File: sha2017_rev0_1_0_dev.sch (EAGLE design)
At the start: 184 parts, among them IC1 AP7215, IC2 CPT112, IC3 CP210X_USB_UART, IC4 ESP32WROOM32, IC5 MCP73833, IC6 FXL6408, Q1 MMBT2222A, Q2 MMBT2222A, Q3 SI1304 BDL, Q4 MOSFET-PCHANNEL, Q5 MMBT2222A, Q6 MOSFET-PCHANNEL, Q7 MMBT2222A, Q8 MMBT2222A, T1 SI2301DS, X1_ JST-PH3, X701 2908-05WB-MG

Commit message: renumbered PCB and placed designators
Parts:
- removed D14: NSVR0320MW2T1G, SparkFun-DiscreteSemi:BAT20JFILM
- removed U$29, U$30: VIA, badge:VIA
- added $$U$7, $$U$9: VIA, badge:VIA
- added D8: NSVR0320MW2T1G, SparkFun-DiscreteSemi:BAT20JFILM
- C1, C5: PARTNO GRM188R71H104KA93D -> (none)
- C10: value 1u -> 100n; PARTNO GRM188R61E105KA12D -> (none)
- C12, C14, C17, C7: value 1u -> 4u7/16V; device rcl:C-EUC0603 -> rcl:C-EUC0805; PARTNO GRM188R61E105KA12D -> GRM21BR61C475KA88K
- C13: value 1u -> 100n; OC_FARNELL (none) -> unknown; PARTNO GRM188R61E105KA12D -> (none)
- C15: value 100n -> 4u7/16V; device rcl:C-EUC0603 -> rcl:C-EUC0805; PARTNO GRM188R71H104KA93D -> GRM21BR61C475KA88K
- C16, C22: value 4u7/16V -> 1u; device rcl:C-EUC0805 -> rcl:C-EUC0603; PARTNO GRM21BR61C475KA88K -> GRM188R61E105KA12D
- C19, C9: value 1u -> 100n; PARTNO GRM188R61E105KA12D -> GRM188R71H104KA93D
- C2, C4: value 4u7/16V -> 100n; device rcl:C-EUC0805 -> rcl:C-EUC0603; PARTNO GRM21BR61C475KA88K -> (none)
- C20: value (none) -> 10uF; device rcl:C-EUC0603 -> rcl:C-EUC0805K; OC_FARNELL unknown -> (none)
- C21: value (none) -> 100nF; device rcl:C-EUC0603 -> rcl:C-EUC0402K; OC_FARNELL unknown -> (none)
- C25: value 10uF -> (none); device rcl:C-EUC0805K -> rcl:C-EUC0603; OC_FARNELL (none) -> unknown
- C26: value 100n -> (none); OC_FARNELL (none) -> unknown
- C27: value 100n -> 4u7/16V; device rcl:C-EUC0603 -> rcl:C-EUC0805; PARTNO (none) -> GRM21BR61C475KA88K
- C28, C29: value 100n -> 1u; PARTNO (none) -> GRM188R61E105KA12D
- C3: device rcl:C-EUC0805 -> 00ralf:C0603-DASHES; PARTNO GRM21BR61C475KA88K -> (none)
- C30: value 100n -> 10uF; device rcl:C-EUC0603 -> rcl:C-EUC0805K
- C31: value 4u7/16V -> 1u; device 00ralf:C0603-DASHES -> rcl:C-EUC0603; PARTNO (none) -> GRM188R61E105KA12D
- C32: value 10uF -> 1u; device rcl:C-EUC0805K -> rcl:C-EUC0603; PARTNO (none) -> GRM188R61E105KA12D
- C33: value 100nF -> 1u; device rcl:C-EUC0402K -> rcl:C-EUC0603; PARTNO (none) -> GRM188R61E105KA12D
- C34: value 100n -> 1u; OC_FARNELL unknown -> (none); PARTNO (none) -> GRM188R61E105KA12D
- C36: value 100n -> 4u7/16V; device rcl:C-EUC0603 -> 00ralf:C0603-DASHES; OC_FARNELL unknown -> (none)
- C37: value 4u7/16V -> (none); device 00ralf:C0603-DASHES -> rcl:C-EUC0603; OC_FARNELL (none) -> unknown
- C38: value (none) -> 100n; OC_FARNELL unknown -> (none); PARTNO (none) -> GRM188R71H104KA93D
- C8: value 4u7/16V -> 100n; device rcl:C-EUC0805 -> rcl:C-EUC0603; OC_FARNELL (none) -> unknown; PARTNO GRM21BR61C475KA88K -> (none)
- D2: PARTNO BAT20JFILM -> (none)
- D3: value NSVR0320MW2T1G -> Yellow; device SparkFun-DiscreteSemi:BAT20JFILM -> SparkFun-LED:LED0603; PARTNO BAT20JFILM -> (none)
- D4: value Yellow -> RED
- D6: value RED -> NSVR0320MW2T1G; device SparkFun-LED:LED0603 -> SparkFun-DiscreteSemi:BAT20JFILM; PARTNO (none) -> BAT20JFILM
- IC1: value AP7215 -> CP210X_USB_UART; device badge:AP7215 -> SparkFun-DigitalIC:CP210X_USB_UART; PARTNO AP7215-33YG-13 -> CP2102-GMR
- IC2: value CPT112 -> AP7215; device badge:CPT112 -> badge:AP7215; PARTNO (none) -> AP7215-33YG-13
- IC3: value CP210X_USB_UART -> ESP32WROOM32; device SparkFun-DigitalIC:CP210X_USB_UART -> ESP3x:ESP32WROOM32; PARTNO CP2102-GMR -> (none)
- IC4: value ESP32WROOM32 -> MCP73833; device ESP3x:ESP32WROOM32 -> SparkFun:MCP73833
- IC5: value MCP73833 -> FXL6408; device SparkFun:MCP73833 -> badge:FXL6408
- IC6: value FXL6408 -> CPT112; device badge:FXL6408 -> badge:CPT112
- Q1: value MMBT2222A -> MOSFET-PCHANNEL; device SparkFun-DiscreteSemi:TRANSISTOR_NPNMMBT2222A -> SparkFun-DiscreteSemi:MOSFET-PCHANNEL; PARTNO BC817-25,215 -> (none)
- Q2: PARTNO BC817-25,215 -> (none)
- Q3: value SI1304 BDL -> MMBT2222A; device SparkFun-DiscreteSemi:MOSFET-NCHANNEL2N7002PW -> SparkFun-DiscreteSemi:TRANSISTOR_NPNMMBT2222A; PARTNO SI1308EDL-T1-GE3 -> (none)
- Q4: value MOSFET-PCHANNEL -> MMBT2222A; device SparkFun-DiscreteSemi:MOSFET-PCHANNEL -> SparkFun-DiscreteSemi:TRANSISTOR_NPNMMBT2222A; PARTNO (none) -> BC817-25,215
- Q5: PARTNO (none) -> BC817-25,215
- Q6: value MOSFET-PCHANNEL -> SI1304 BDL; device SparkFun-DiscreteSemi:MOSFET-PCHANNEL -> SparkFun-DiscreteSemi:MOSFET-NCHANNEL2N7002PW; PARTNO (none) -> SI1308EDL-T1-GE3
- Q8: value MMBT2222A -> MOSFET-PCHANNEL; device SparkFun-DiscreteSemi:TRANSISTOR_NPNMMBT2222A -> SparkFun-DiscreteSemi:MOSFET-PCHANNEL
- R1: value 1k -> 10R; device rcl:R-EU_R0603 -> 00ralf:R0603-DASHES; PARTNO ERJ-3GEYJ102V -> (none)
- R10: value 100k -> 10k; PARTNO CRCW0603100KFKEA -> ERJ-3GEYJ103V
- R11: value 10k -> 1k; device 00ralf:R0603-DASHES -> rcl:R-EU_R0603; PARTNO (none) -> ERJ-3GEYJ102V
- R12: value 10R -> 10k; device 00ralf:R0603-DASHES -> rcl:R-EU_R0603; PARTNO (none) -> ERJ-3GEYJ103V
- R13: device 00ralf:R0603-DASHES -> rcl:R-EU_R0603; PARTNO (none) -> ERJ-3GEYJ103V
- R14: value 2.2k -> 10k; PARTNO (none) -> ERJ-3GEYJ103V
- R15: value 1k -> 5R; device rcl:R-EU_R0603 -> 00ralf:R0603-DASHES; PARTNO (none) -> ERJ-3GEYJ5R1V
- R16: value 10k -> 100k
- R18: device 00ralf:R0603-DASHES -> rcl:R-EU_R0603; OC_FARNELL (none) -> unknown; PARTNO (none) -> ERJ-3GEYJ103V
- R19: value 10k -> 470R; device 00ralf:R0603-DASHES -> rcl:R-EU_R0603; OC_FARNELL (none) -> unknown; PARTNO (none) -> ERJ-3GEYJ103V
- R20: value 100k -> 470R; OC_FARNELL (none) -> unknown; PARTNO (none) -> ERJ-3GEYJ103V
- R21: value 220k -> 10k; device rcl:R-EU_R0603 -> 00ralf:R0603-DASHES
- R22: value 100k -> 10k; device rcl:R-EU_R0603 -> 00ralf:R0603-DASHES
- R23: value 150k -> 2.2k
- R25: value 10k -> 100k; device 00ralf:R0603-DASHES -> rcl:R-EU_R0603; PARTNO (none) -> CRCW0603100KFKEA
- R26: value 10k -> 150k; OC_FARNELL unknown -> (none); PARTNO ERJ-3GEYJ103V -> (none)
- R27: value 470R -> 10k
- R28: value 470R -> 1k; OC_FARNELL unknown -> (none); PARTNO ERJ-3GEYJ103V -> (none)
- R3: PARTNO ERJ-3GEYJ103V -> (none)
- R4: value 1k -> 100k; PARTNO ERJ-3GEYJ102V -> (none)
- R5: value 10k -> 220k; PARTNO ERJ-3GEYJ103V -> (none)
- R6: device rcl:R-EU_R0603 -> 00ralf:R0603-DASHES; PARTNO ERJ-3GEYJ103V -> (none)
- R7: value 5R -> 10k; PARTNO ERJ-3GEYJ5R1V -> (none)
- R8: device rcl:R-EU_R0603 -> 00ralf:R0603-DASHES; OC_FARNELL unknown -> (none); PARTNO ERJ-3GEYJ103V -> (none)
- R9: value 10k -> 1k; PARTNO ERJ-3GEYJ103V -> ERJ-3GEYJ102V
- renumbered D10 to D101, D11 to D102, D12 to D103, D13 to D104, D9 to D100, J3 to J2, TB1 to TB104, TB2 to TB103, TB3 to TB101, TB4 to TB100, TB5 to TB102, TP10 to TP107, TP11 to TP106, TP12 to TP104, TP13 to TP105, TP14 to TP131, TP15 to TP130, TP16 to TP129, TP17 to TP127, TP18 to TP126, TP19 to TP125, TP20 to TP113, TP22 to TP114, TP23 to TP119, TP24 to TP120, TP25 to TP116, TP26 to TP115, TP27 to TP109, TP28 to TP118, TP29 to TP128, TP3 to TP100, TP30 to TP111, TP31 to TP132, TP32 to TP121, TP33 to TP133, TP34 to TP134, TP35 to TP137, TP36 to TP138, TP37 to TP108, TP38 to TP103, TP39 to TP124, TP4 to TP101, TP40 to TP135, TP41 to TP139, TP42 to TP102, TP43 to TP136, TP5 to TP123, TP6 to TP122, TP7 to TP117, TP8 to TP112, TP9 to TP110, U$31 to $$U$8, X1_ to X1, X701 to X2
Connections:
- net +3V3: now also C14.1, C17.1, C27.1, C34.1, C37.1, IC2.OUT, IC3.VCC, IC5.ADDR, IC5.VCC, IC5.VDDIO, IC6.VDD, Q8.D, R13.2, R18.1, R19.1, R20.1, R22.2, R25.1, R28.2; no longer C16.1, C22.1, C35.1, C4.1, C5.1, IC1.OUT, IC2.VDD, IC4.VCC, IC6.ADDR, IC6.VCC, IC6.VDDIO, Q6.D, R10.1, R24.2, R25.2, R26.1, R28.1, R8.1, R9.2
- net +5V: now also C20.2, C21.2, C7.1, C9.1, D2.A, IC1.REGIN, IC1.VBUS, IC4.VDD@1, IC4.VDD@2, R3.2, R5.2; no longer C11.1, C2.1, C32.2, C33.2, D14.A, IC3.REGIN, IC3.VBUS, IC5.VDD@1, IC5.VDD@2, R16.2, R21.2
- net 3V3_SWITCHED: now also C35.1, C36.1, Q8.S; no longer C15.1, C37.1, Q6.S
- net CHRG_STAT: now also IC4.STAT1, IC5.GPIO0; no longer IC5.STAT1, IC6.GPIO0
- net ESP32_!RESET: now also IC3.EN, Q4.C, R18.2, S1.2; no longer IC4.EN, Q1.C, R8.2, S2.2
- net ESP32_FLASH: now also IC3.IO0, Q5.C, R13.1, S2.2; no longer IC4.IO0, Q2.C, R9.1, S1.2
- net ESP32_RX: now also D3.C, IC1.TXD, IC3.RXD0; no longer D4.C, IC3.TXD, IC4.RXD0
- net ESP32_TX: now also D4.C, IC1.RXD, IC3.TXD0; no longer D6.C, IC3.RXD, IC4.TXD0
- net EXTIO-0: now also IC3.IO33; no longer IC4.IO33
- net EXTIO-1: now also IC3.IO16; no longer IC4.IO16
- net EXTIO-2: now also IC3.IO17; no longer IC4.IO17
- net EXTIO-3: now also IC5.GPIO7; no longer IC6.GPIO7
- net EXTIO-4: now also IC5.GPIO6; no longer IC6.GPIO6
- net EXTIO-5: now also IC5.GPIO5; no longer IC6.GPIO5
- net GDR: now also Q6.G; no longer Q3.G
- net GND: now also $$U$7.P$1, $$U$9.P$1, C1.1, C12.2, C13.2, C14.2, C16.1, C17.2, C2.1, C27.2, C31.1, C4.1, C5.1, C7.2, C9.2, D6.C, IC1.GND@EXP, IC1.GND@M, IC3.GND@0, IC3.GND@1, IC3.GND@3, IC4.VSS, IC5.GND, Q2.E, Q3.E, R15.2, R26.1, R3.1, R4.1; no longer C1.2, C12.1, C13.1, C16.2, C17.1, C2.2, C22.2, C27.1, C31.2, C4.2, C5.2, C7.1, C9.1, D3.C, IC3.GND@EXP, IC3.GND@M, IC4.GND, IC4.GND@0, IC4.GND@1, IC4.GND@3, IC5.VSS, Q5.E, Q8.E, R14.1, R20.1, R22.1, R7.2, U$29.P$1, U$30.P$1
- net I2C_INT: now also IC3.IO25, IC5.INT; no longer IC4.IO25, IC6.INT
- net I2C_SCL: now also IC3.IO27, IC5.SCL, IC6.EB_SCL, R20.2; no longer IC2.EB_SCL, IC4.IO27, IC6.SCL, R27.2
- net I2C_SDA: now also IC3.IO26, IC5.SDA, IC6.EB_SDA, R19.2; no longer IC2.EB_SDA, IC4.IO26, IC6.SDA, R28.2
- net LCD_!RESET: now also IC3.IO23; no longer IC4.IO23
- net LCD_BUSY: now also IC3.IO22; no longer IC4.IO22
- net LCD_CS: now also IC3.IO19; no longer IC4.IO19
- net LCD_D/!S: now also IC3.IO21; no longer IC4.IO21
- net LCD_MOSI: now also IC3.IO5; no longer IC4.IO5
- net LCD_SCK: now also IC3.IO18; no longer IC4.IO18
- net N$1: now also IC6.CS11/BUZZ; no longer IC2.CS11/BUZZ
- net N$10: now also IC1.RTS, Q4.E, R12.1; no longer IC3.RTS, Q1.E, R5.1
- net N$11: now also IC1.DTR, Q5.E, R14.1; no longer IC3.DTR, Q2.E, R6.1
- net N$12: now also IC3.SD1; no longer IC4.SD1
- net N$13: now also Q5.B, R12.2; no longer Q2.B, R5.2
- net N$14: now also Q4.B, R14.2; no longer Q1.B, R6.2
- net N$15: now also Q7.B, R21.2; no longer Q8.B, R11.2
- net N$16: now also Q3.C; no longer Q7.C
- net N$17: now also Q7.C, Q8.G, R22.1; no longer Q6.G, Q8.C, R25.1
- net N$18: now also R1.1; no longer R12.1
- net N$22: now also C22.1, D6.A, D7.C; no longer C14.1, D2.C, D3.A
- net N$23: now also C22.2, D8.A, Q6.D; no longer C14.2, D7.A, Q3.D
- net N$25: now also IC6.CS02; no longer IC2.CS02
- net N$26: now also R9.1; no longer R2.1
- net N$27: now also D3.A, R2.1; no longer D4.A, R1.1
- net N$28: now also D4.A, R11.1; no longer D6.A, R4.1
- net N$3: now also IC3.SD2; no longer IC4.SD2
- net N$4: now also IC3.SD3; no longer IC4.SD3
- net N$42: now also C25.2, IC3.SENSOR_VP; no longer C20.2, IC4.SENSOR_VP
- net N$43: now also C26.2, IC3.SENSOR_VN; no longer C21.2, IC4.SENSOR_VN
- net N$45: now also Q3.B, R8.1; no longer Q7.B, R13.1
- net N$46: now also IC4.PROG, R23.2; no longer IC5.PROG, R14.2
- net N$47: now also IC4.THERM, R24.2; no longer IC5.THERM, R15.2
- net N$48: now also R24.1, R26.2; no longer R15.1, R23.2
- net N$49: now also C30.2, IC4.VBAT@1, IC4.VBAT@2; no longer C25.2, IC5.VBAT@1, IC5.VBAT@2
- net N$52: now also Q2.B, R7.2; no longer Q5.B, R18.2
- net N$53: now also Q1.G, Q2.C, R6.1; no longer Q4.G, Q5.C, R19.1
- net N$55: now also IC6.CS03; no longer IC2.CS03
- net N$56: now also IC6.CS04; no longer IC2.CS04
- net N$57: now also IC6.CS05; no longer IC2.CS05
- net N$58: now also IC6.CS09; no longer IC2.CS09
- net N$59: now also IC5.!RESET, R27.2; no longer IC6.!RESET, R26.2
- net N$6: now also IC3.CND; no longer IC4.CND
- net N$61: now also IC6.CONF_CLK/RST, R28.1, TP2.1; no longer IC2.CONF_CLK/RST, R24.1, TP1.1
- net N$62: now also IC6.CONF_DAT, TP1.1; no longer IC2.CONF_DAT, TP2.1
- net N$64: now also IC6.CS08; no longer IC2.CS08
- net N$65: now also IC6.CS07; no longer IC2.CS07
- net N$7: now also IC3.CLK; no longer IC4.CLK
- net N$8: now also IC1.!RST, R10.2; no longer IC3.!RST, R3.2
- net N$9: now also IC3.SD0; no longer IC4.SD0
- net PREVGH: now also C28.2, D8.C; no longer C13.2, D7.C
- net PREVGL: now also C32.2, D7.A; no longer C9.2, D2.A
- net PROXIMITY: now also IC6.CS00; no longer IC2.CS00
- net RESE: now also Q6.S, R15.1; no longer Q3.S, R7.1
- net SD_CD: now also IC5.GPIO4, R25.2; no longer IC6.GPIO4, R10.2
- net SD_CLK: now also IC3.IO14; no longer IC4.IO14
- net SD_CMD: now also IC3.IO15; no longer IC4.IO15
- net SD_DATA0: now also IC3.IO2; no longer IC4.IO2
- net SD_DATA1: now also IC3.IO4; no longer IC4.IO4
- net SD_DATA2: now also IC3.IO12; no longer IC4.IO12
- net SD_DATA3: now also IC3.IO13; no longer IC4.IO13
- net TOUCH_INT: now also IC5.GPIO3, IC6.EB_INT; no longer IC2.EB_INT, IC6.GPIO3
- net USB_DN_CON: now also IC1.D-; no longer IC3.D-
- net USB_DP_CON: now also IC1.D+; no longer IC3.D+
- net VBAT_SENSE: now also C13.1, IC3.IO35, R16.2; no longer C34.1, IC4.IO35, R20.2
- net VCC: now also C11.1, C12.1, C15.1, D2.C, IC2.IN, Q1.D, R1.2, R6.2; no longer C1.1, C3.1, C8.1, D14.C, IC1.IN, Q4.D, R12.2, R19.2
- net VCOM: now also C33.2; no longer C7.2
- net VDD: now also IC1.VDD, R10.1, R11.2, R9.2; no longer IC3.VDD, R1.2, R3.1, R4.2
- net VGH: now also C18.2; no longer C17.2
- net VGL: now also C16.2; no longer C18.2
- net VIBRATOR: now also IC5.GPIO1, R8.2; no longer IC6.GPIO1, R13.2
- net VSH: now also C29.2; no longer C12.2
- net VSL: now also C31.2; no longer C10.2
- net VUSB_SENSE: now also C8.1, IC3.IO34, R4.2, R5.1; no longer C36.1, IC4.IO34, R21.1, R22.2
- net WS2812_DATA: now also IC3.IO32; no longer IC4.IO32
- net WS2812_POWER: now also C1.2, C10.2, C2.2, C3.1, C4.2, C5.2, Q1.S; no longer C26.2, C27.2, C28.2, C29.2, C30.2, C31.1, Q4.S
- net WS2812_POWER_EN: now also IC5.GPIO2, R21.1, R7.1; no longer IC6.GPIO2, R11.1, R18.1

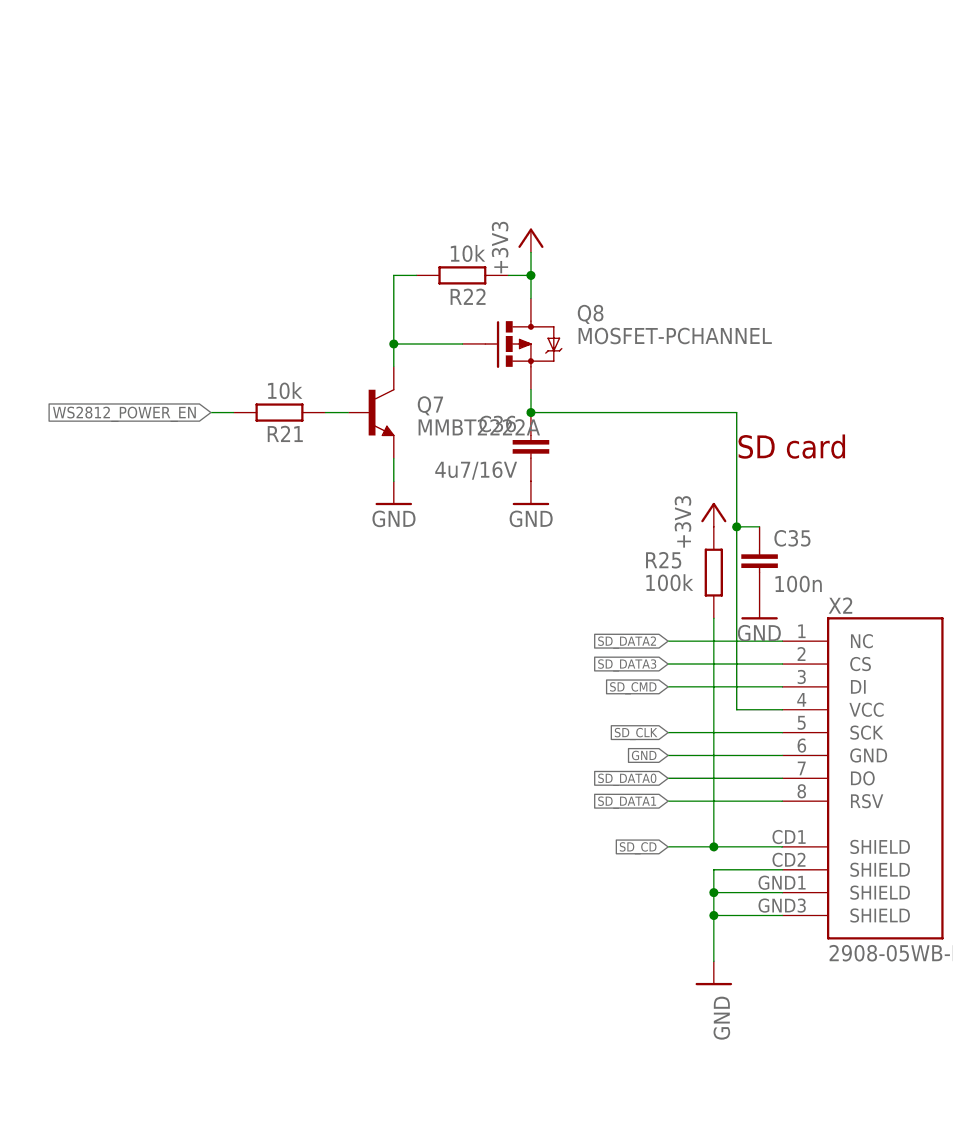
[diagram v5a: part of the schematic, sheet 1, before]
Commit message: added SDIO pullups and some bootstrap magic for it
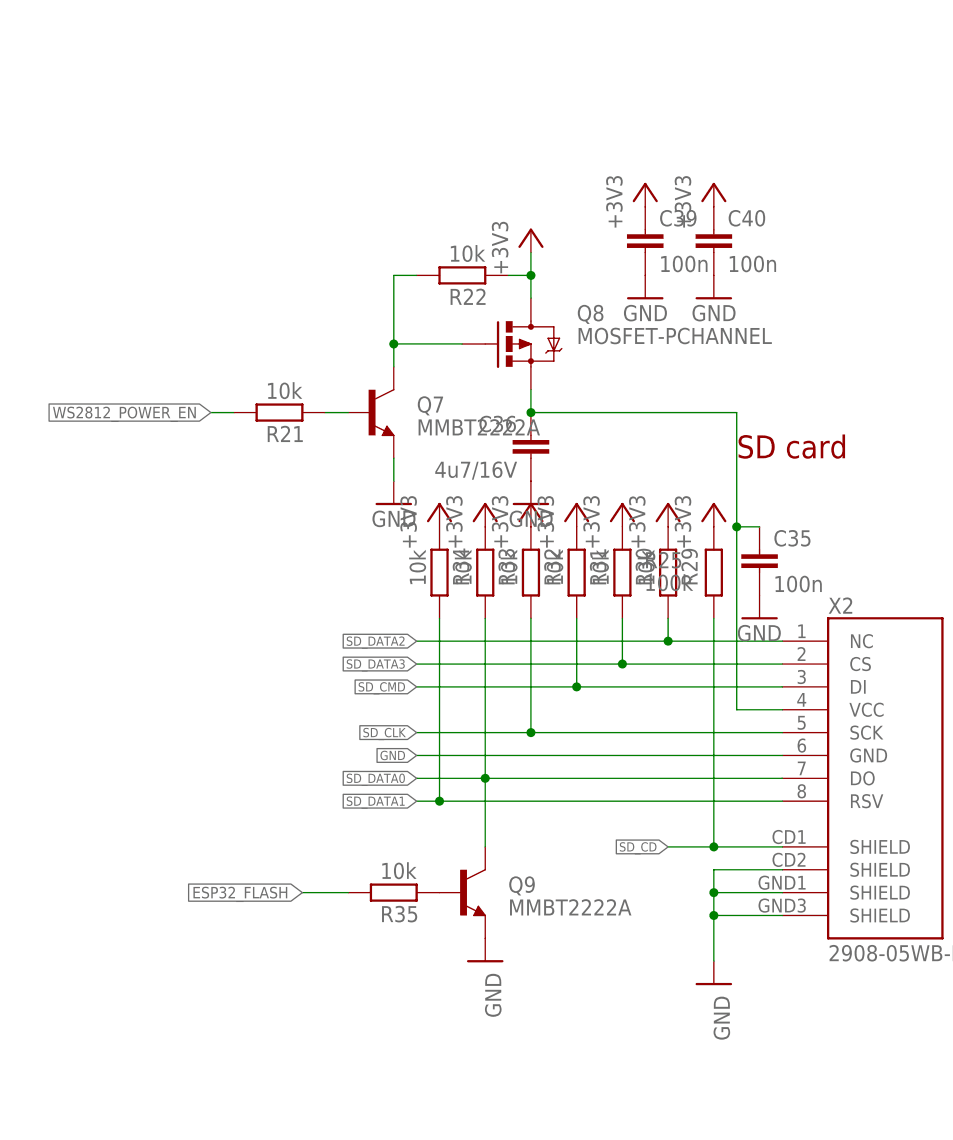
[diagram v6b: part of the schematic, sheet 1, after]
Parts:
- added C39, C40: 100n, rcl:C-EUC0603
- added Q9: MMBT2222A, SparkFun-DiscreteSemi:TRANSISTOR_NPNMMBT2222A
- added R29, R30, R31, R32, R33, R34, R35: 10k, 00ralf:R0603-DASHES
- renumbered J2 to X3
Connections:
- new net N$20: Q9.B, R35.2
- net +3V3: now also C39.1, C40.1, R29.2, R30.2, R31.2, R32.2, R33.2, R34.2
- net ESP32_FLASH: now also R35.1
- net GND: now also C39.2, C40.2, Q9.E
- net SD_CLK: now also R32.1
- net SD_CMD: now also R31.1
- net SD_DATA0: now also Q9.C, R33.1
- net SD_DATA1: now also R34.1
- net SD_DATA2: now also R29.1
- net SD_DATA3: now also R30.1

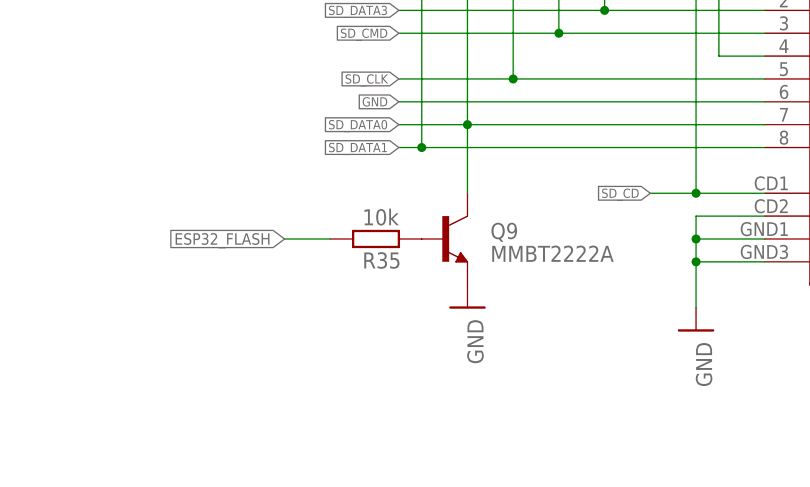
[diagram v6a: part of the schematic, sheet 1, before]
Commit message: replaced transistor with a diode becaus we need it non inverting
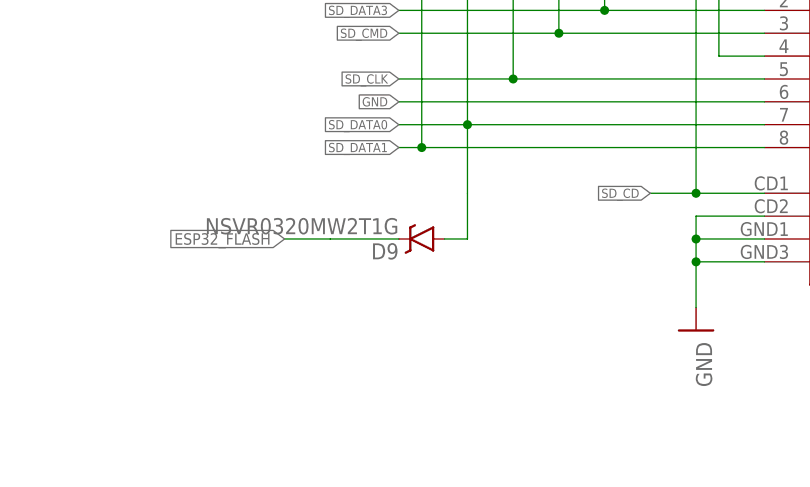
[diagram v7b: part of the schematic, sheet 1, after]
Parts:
- removed Q9: MMBT2222A, SparkFun-DiscreteSemi:TRANSISTOR_NPNMMBT2222A
- removed R35: 10k, 00ralf:R0603-DASHES
- added D9: NSVR0320MW2T1G, SparkFun-DiscreteSemi:BAT20JFILM
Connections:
- removed net N$20: Q9.B, R35.2
- net ESP32_FLASH: now also D9.C; no longer R35.1
- net GND: no longer Q9.E
- net SD_DATA0: now also D9.A; no longer Q9.C
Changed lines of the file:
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@@
 <part name="+3V14" library="supply1" deviceset="+3V3" device=""/>
 <part name="+3V15" library="supply1" deviceset="+3V3" device=""/>
-<part name="Q9" library="SparkFun-DiscreteSemi" deviceset="TRANSISTOR_NPN" device="MMBT2222A" value="MMBT2222A"/>
-<part name="GND90" library="supply1" deviceset="GND" device=""/>
-<part name="R35" library="00ralf" deviceset="R0603-DASHES" device="" value="10k"/>
 <part name="C39" library="rcl" deviceset="C-EU" device="C0603" value="100n">
 <attribute name="PARTNO" value="GRM188R71H104KA93D"/>
@@
 <part name="GND91" library="supply1" deviceset="GND" device=""/>
 <part name="GND92" library="supply1" deviceset="GND" device=""/>
+<part name="D9" library="SparkFun-DiscreteSemi" deviceset="BAT20JFILM" device="" value="NSVR0320MW2T1G">
+<attribute name="PARTNO" value="BAT20JFILM"/>
+</part>
 </parts>
 <sheets>
@@
 <instance part="+3V14" gate="G$1" x="134.62" y="76.2"/>
 <instance part="+3V15" gate="G$1" x="129.54" y="76.2"/>
-<instance part="Q9" gate="G$1" x="132.08" y="33.02"/>
-<instance part="GND90" gate="1" x="134.62" y="25.4" smashed="yes">
-<attribute name="VALUE" x="134.62" y="24.13" size="1.778" layer="96" rot="R270"/>
-</instance>
-<instance part="R35" gate="G$1" x="124.46" y="33.02" smashed="yes" rot="MR180">
-<attribute name="NAME" x="127.254" y="31.5214" size="1.778" layer="95" rot="R180"/>
-<attribute name="VALUE" x="127" y="36.322" size="1.778" layer="96" rot="R180"/>
-</instance>
 <instance part="C39" gate="G$1" x="152.4" y="106.68">
 <attribute name="PARTNO" x="152.4" y="106.68" size="1.778" layer="96" rot="MR0" display="off"/>
@@
 <instance part="GND91" gate="1" x="152.4" y="99.06" rot="MR0"/>
 <instance part="GND92" gate="1" x="160.02" y="99.06" rot="MR0"/>
+<instance part="D9" gate="G$1" x="129.54" y="33.02" rot="R180">
+<attribute name="PARTNO" x="129.54" y="33.02" size="1.778" layer="96" rot="MR270" display="off"/>
+</instance>
 </instances>
 <busses>
@@
 <wire x1="327.66" y1="63.5" x2="325.12" y2="63.5" width="0.1524" layer="91"/>
 <wire x1="325.12" y1="63.5" x2="325.12" y2="60.96" width="0.1524" layer="91"/>
-</segment>
-<segment>
-<pinref part="Q9" gate="G$1" pin="E"/>
-<pinref part="GND90" gate="1" pin="GND"/>
 </segment>
 <segment>
@@
 </segment>
 <segment>
-<pinref part="R35" gate="G$1" pin="1"/>
 <wire x1="119.38" y1="33.02" x2="114.3" y2="33.02" width="0.1524" layer="91"/>
 <label x="114.3" y="33.02" size="1.27" layer="95" rot="R180" xref="yes"/>
+<pinref part="D9" gate="G$1" pin="C"/>
+<wire x1="119.38" y1="33.02" x2="127" y2="33.02" width="0.1524" layer="91"/>
 </segment>
 </net>
@@
 <wire x1="134.62" y1="63.5" x2="134.62" y2="45.72" width="0.1524" layer="91"/>
 <junction x="134.62" y="45.72"/>
-<pinref part="Q9" gate="G$1" pin="C"/>
 <wire x1="134.62" y1="45.72" x2="134.62" y2="38.1" width="0.1524" layer="91"/>
+<pinref part="D9" gate="G$1" pin="A"/>
+<wire x1="132.08" y1="33.02" x2="134.62" y2="33.02" width="0.1524" layer="91"/>
+<wire x1="134.62" y1="33.02" x2="134.62" y2="38.1" width="0.1524" layer="91"/>
 </segment>
 </net>
@@
 </segment>
 </net>
-<net name="N$20" class="0">
-<segment>
-<pinref part="Q9" gate="G$1" pin="B"/>
-<pinref part="R35" gate="G$1" pin="2"/>
-</segment>
-</net>
